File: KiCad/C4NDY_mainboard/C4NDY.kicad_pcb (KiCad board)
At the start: 2 copper layers, 22.9 x 50.2 mm, 46 parts, among them J1 Conn_01x08, J2 Conn_01x07, J3 Conn_01x05, J4 5077CR-16SMC2-BK-TR, J5 Conn_01x06, J6 Conn_01x08, J7 FTSH-105-01-L-DV-K, SW1 SKRPABE010, SW2 SKRPABE010, U1 MIC39100-3.3WS, U2 IS66WVS2M8BLL, U3 STM32G4A1CETx, X1 SG-310SCF

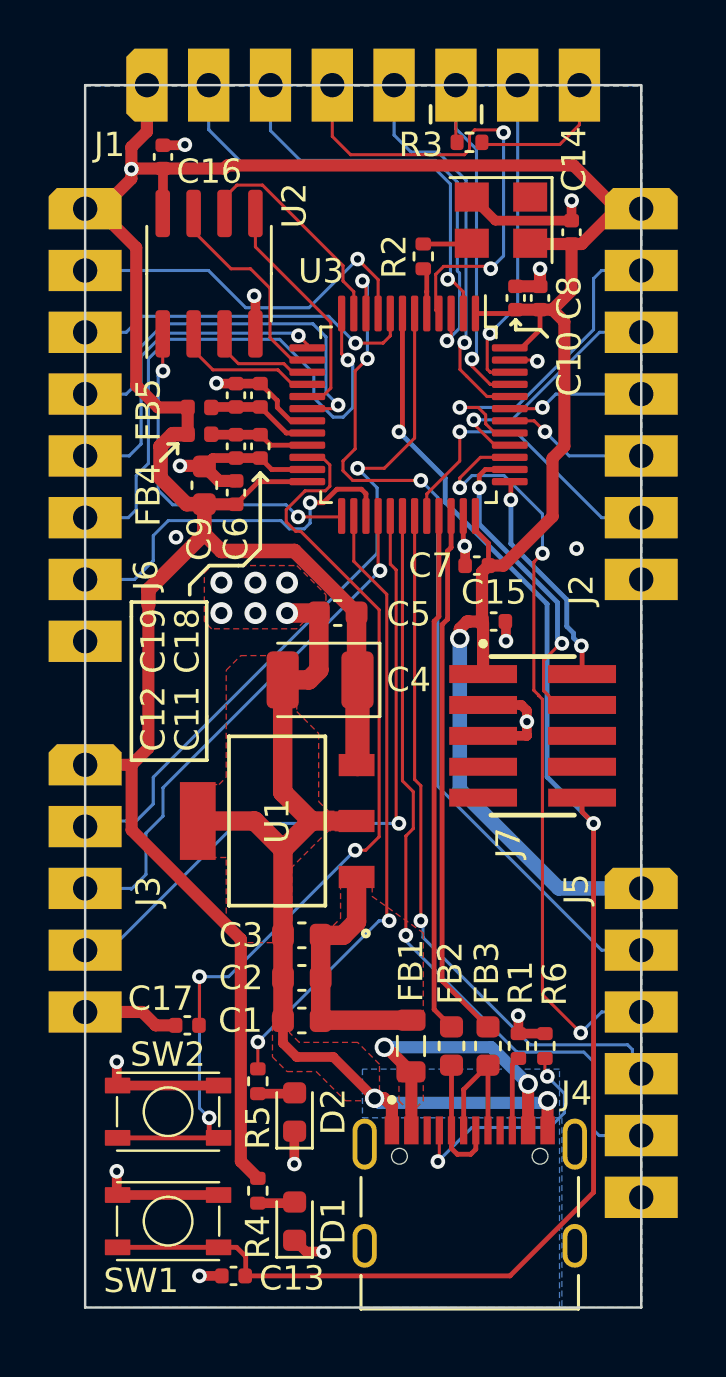
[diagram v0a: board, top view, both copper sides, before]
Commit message: SWD用のコネクタを汎用のピンヘッダに変更し、viaをテントに修正。
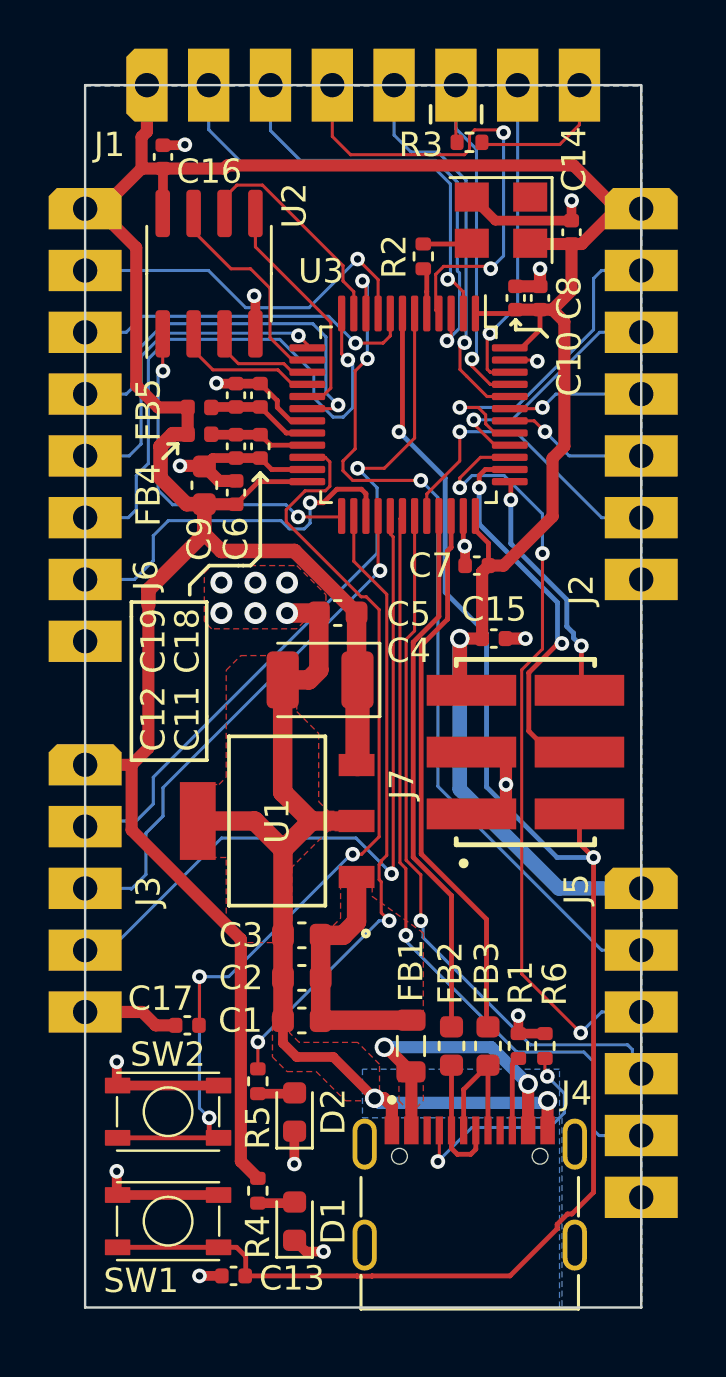
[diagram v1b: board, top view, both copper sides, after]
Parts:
- J4: value 5077CR-16SMC2-BK-TR -> UB1611-HGN; footprint My_Parts:NELTRON_5077CR-16SMC2-BK-TR -> My_Parts:Gangyuan_UB1611-HGN
- J7: value FTSH-105-01-L-DV-K -> 15910060; footprint My_Parts:SAMTEC_FTSH-105-XX-X-DV -> My_Parts:Molex_15910060
- moved J7 0.73 mm to (148.1, 107.2), turned to 90 degrees
- moved G*** 0.71 mm to (141.2, 104.4)
- moved C15 0.70 mm to (146.8, 102.5)
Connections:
- J7 pad 1: VCC -> GND
- J7 pad 2: /SWDIO -> /NRST
- J7 pad 5: GND -> VCC
- J7 pad 6: unconnected-(J7-Pin_6-Pad6) -> /SWDIO
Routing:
- net /SWCLK: track 13.5 -> 16.1 mm
- net /SPI_MOSI: track 26.8 -> 28.9 mm
- net /NRST: track 63.3 -> 65.1 mm
- net /SWDIO: track 9.14 -> 9.87 mm
- net /USB_DP: track 21.9 -> 22.6 mm
- net /USB_DM: track 21.8 -> 22.5 mm
- net GND: track 97.7 -> 98.3 mm, vias 26 -> 24
- net VCC: track 142.9 -> 142.7 mm, vias 2 -> 1
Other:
- board text added: "NRST"
- board text added: "SWCLK"
- board text added: "SWDIO"
- board text added: "VCC"
- board text added: "rev.D"
- board text removed: "SWD"
- board text removed: "rev.C"

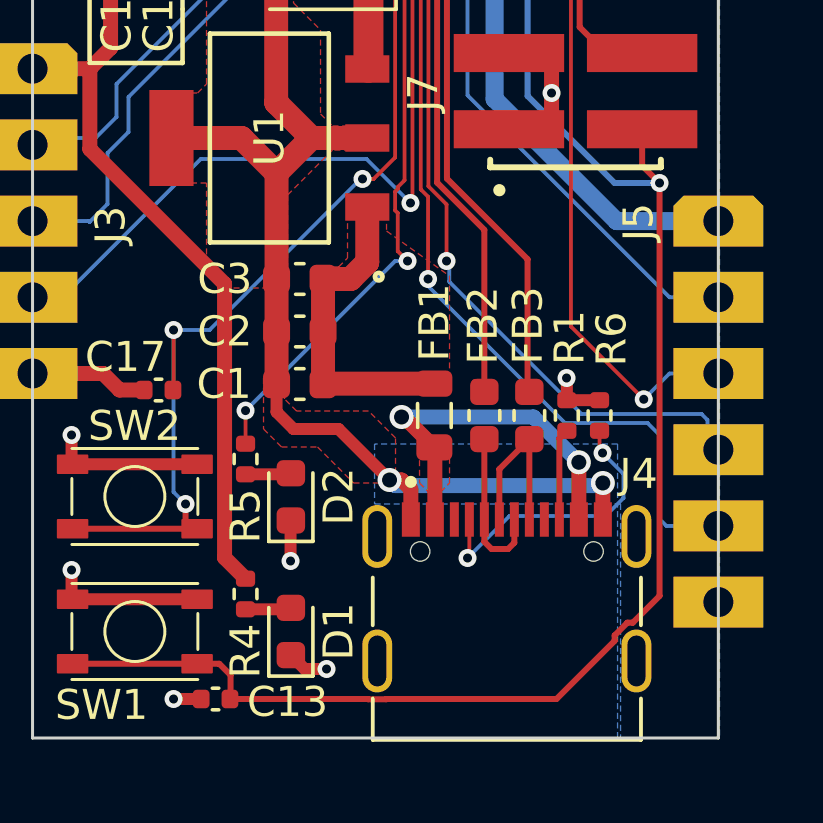
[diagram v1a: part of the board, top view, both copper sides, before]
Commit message: Modify USB Type-C Connector Position.
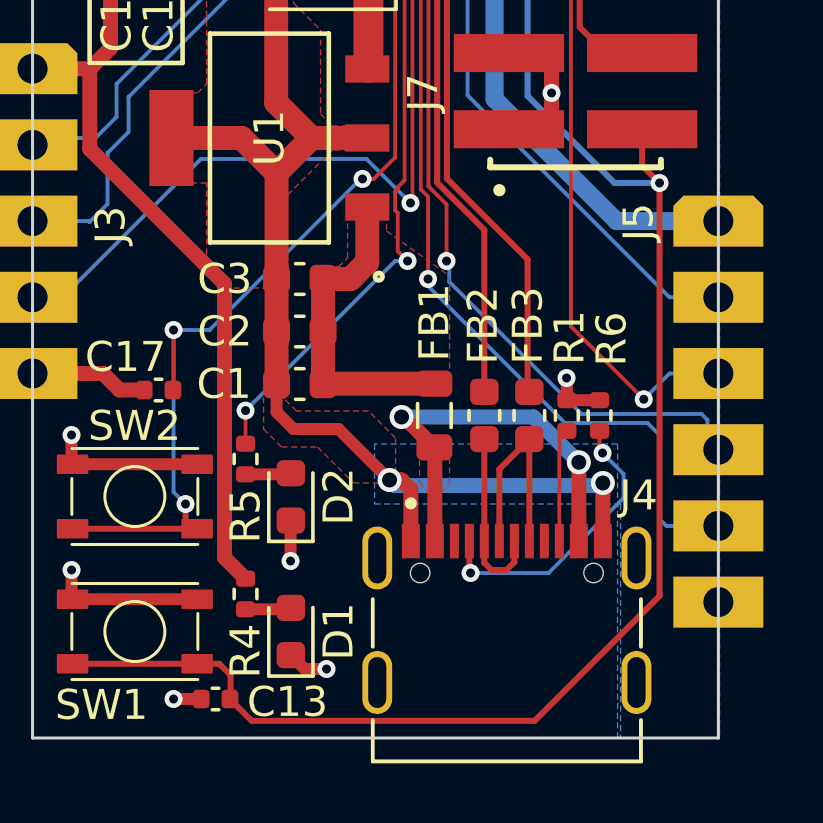
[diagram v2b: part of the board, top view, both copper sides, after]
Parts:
- moved J4 0.72 mm to (145.8, 124.5)
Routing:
- net GND: track 98.3 -> 100.3 mm
- net Net-(FB1-Pad1): track 12.4 -> 13.8 mm
- net /DP: track 5.77 -> 7.21 mm
- net Net-(J4-CC2): track 3.06 -> 3.78 mm
- net /DN: track 5.38 -> 6.04 mm
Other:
- board text added: "rev.F"
- board text removed: "rev.D"

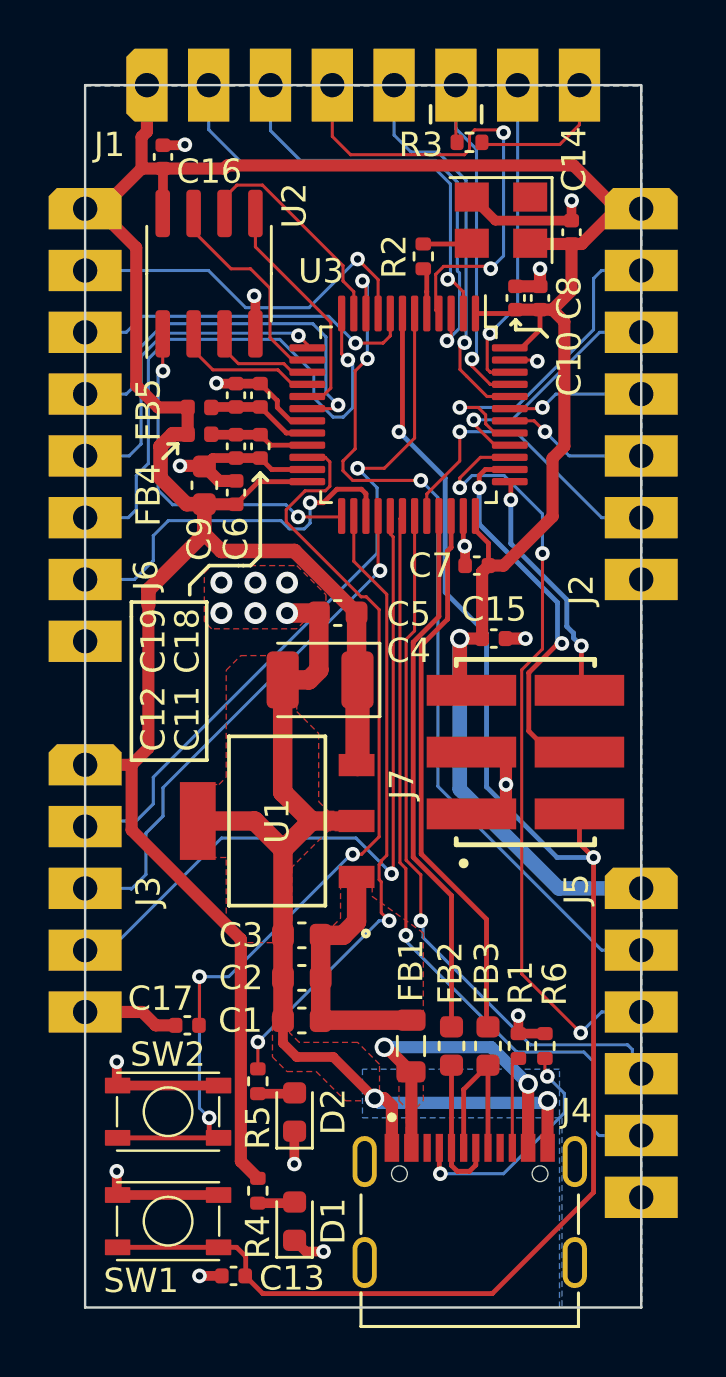
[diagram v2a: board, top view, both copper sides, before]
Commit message: Added TPS2116 and removed onboard QSPI..
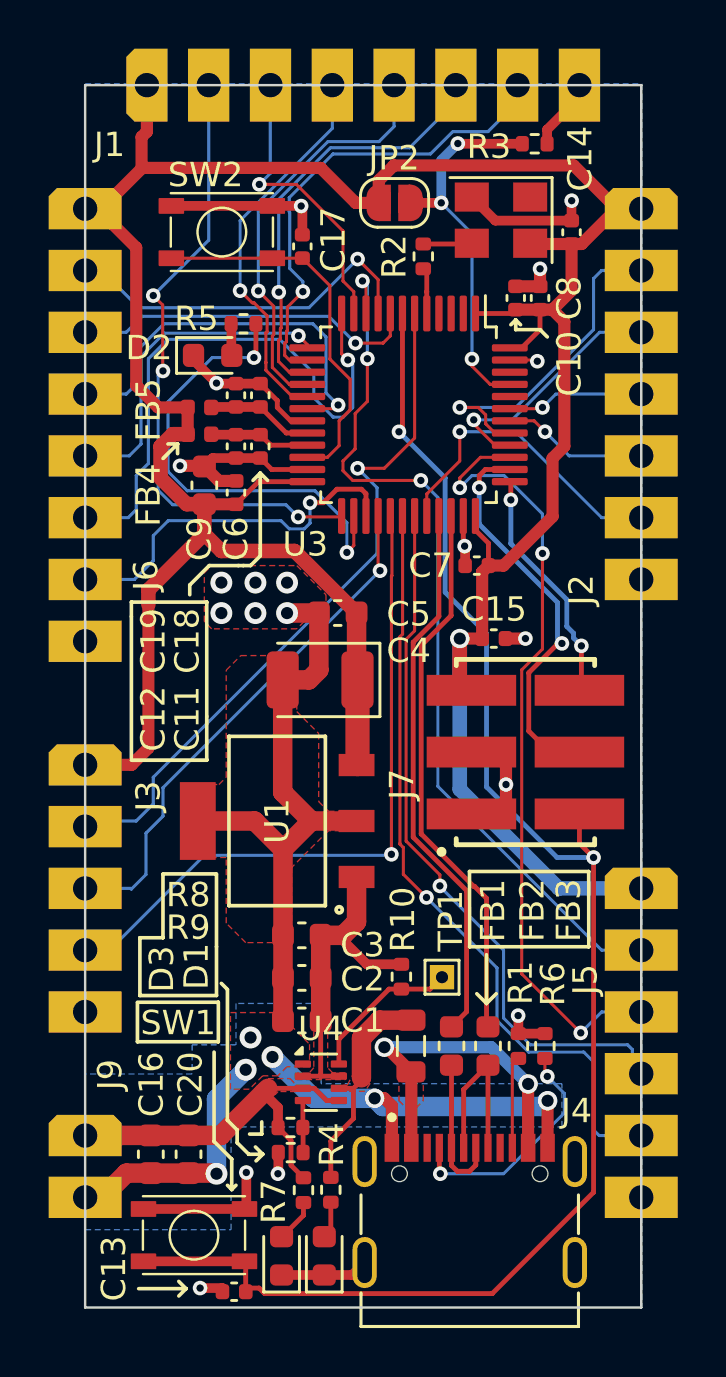
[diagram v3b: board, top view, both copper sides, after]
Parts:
- removed U2: IS66WVS2M8BLL, Package_SO:SOIC-8_3.9x4.9mm_P1.27mm
- added C20: 100nF, Capacitor_SMD:C_0603_1608Metric, F.Cu at (134.2, 123.7)
- added D3: LED, LED_SMD:LED_0603_1608Metric, F.Cu at (138.1, 127.9)
- added J9: Conn_01x02, My_Parts:PinHeader_1x02_P2.54mm_Vertical, F.Cu at (130.0, 122.9)
- added JP2: Jumper_2_Open, Jumper:SolderJumper-2_P1.3mm_Open_RoundedPad1.0x1.5mm, F.Cu at (142.7, 84.6)
- added R10: 10k, Resistor_SMD:R_0402_1005Metric, F.Cu at (143.0, 116.4)
- added R7: 1k, Resistor_SMD:R_0402_1005Metric, F.Cu at (139.0, 125.2)
- added R8: 16.9k, Resistor_SMD:R_0402_1005Metric, F.Cu at (138.4, 122.6)
- added R9: 5k, Resistor_SMD:R_0402_1005Metric, F.Cu at (138.4, 123.6)
- added TP1: TestPoint, TestPoint:TestPoint_THTPad_1.0x1.0mm_Drill0.5mm, F.Cu at (144.7, 116.4)
- added U4: TPS2116DRL, My_Parts:SOT-583-8, F.Cu at (139.7, 120.7)
- C16: value 100nF -> 10uF; footprint Capacitor_SMD:C_0402_1005Metric -> Capacitor_SMD:C_0603_1608Metric
- moved C16 41.0 mm to (132.7, 123.7), turned to -90 degrees
- moved SW2 36.2 mm to (135.6, 85.8)
- moved C17 32.4 mm to (138.9, 86.4), turned to 90 degrees
- moved D2 31.3 mm to (135.2, 90.9), turned to 0 degrees
- moved R5 31.1 mm to (136.5, 89.6), turned to 180 degrees
- moved R4 3.00 mm to (140.1, 125.2)
- moved R3 2.68 mm to (148.5, 82.2)
- moved D1 1.88 mm to (139.8, 127.9)
- moved SW1 1.21 mm to (134.5, 127.0)
- moved C13 0.65 mm to (136.1, 129.3)
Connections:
- C16 pad 1: VCC -> /PWR
- FB1 pad 2: VDD -> VBUS
- J1 pad 2: /PC13 -> /QSPI_NCS
- J1 pad 3: /PC14 -> /QSPI_CLK
- J1 pad 4: /PC15 -> /QSPI_IO0
- J1 pad 5: /PB7 -> /QSPI_IO1
- J1 pad 6: /BOOT0 -> /QSPI_IO2
- J1 pad 7: /PB9 -> /QSPI_IO3
- R4 pad 1: VCC -> VBUS
- U3 pad 2: /PC13 -> unconnected-(U3-PC13-Pad2)
- U3 pad 3: /PC14 -> unconnected-(U3-PC14-Pad3)
- U3 pad 4: /PC15 -> unconnected-(U3-PC15-Pad4)
- U3 pad 44: /PB7 -> unconnected-(U3-PB7-Pad44)
- U3 pad 46: /PB9 -> unconnected-(U3-PB9-Pad46)
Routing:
- net Net-(SW2-A): track 42.1 -> 15.6 mm, vias 3 -> 0
- net /PC15: track 19.8 -> 0.00 mm, vias 2 -> 0
- net VCC: track 142.7 -> 123.5 mm
- net /PC13: track 17.4 -> 0.00 mm, vias 1 -> 0
- net /PC14: track 17.4 -> 0.00 mm, vias 1 -> 0
- net /PB7: track 15.8 -> 0.00 mm, vias 1 -> 0
- net /PWR: track 0.00 -> 14.9 mm
- net /QSPI_IO2: track 4.44 -> 17.0 mm, vias 0 -> 1
- net /PB9: track 12.2 -> 0.00 mm, vias 1 -> 0
- net /QSPI_NCS: track 14.5 -> 25.7 mm, vias 2 -> 3
- net /QSPI_IO1: track 5.93 -> 16.9 mm, vias 0 -> 1
- net /QSPI_IO3: track 8.79 -> 19.4 mm, vias 0 -> 1
- net VBUS: track 0.00 -> 9.16 mm
- net GND: track 100.3 -> 107.1 mm, vias 24 -> 25
- net /QSPI_IO0: track 9.57 -> 16.2 mm, vias 0 -> 1
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- added copper zone on F.Cu, net /PWR
- added copper zone on F.Cu, net VBUS
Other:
- board text added: "15"
- board text added: "16"
- board text added: "21"
- board text added: "22"
- board text added: "28"
- board text added: "29"
- board text added: "36"
- board text added: "[PWR] VIN:14(5V only) VCC:1,9,21,28,36 GND:8,13,15,16,22,29 [ADC] 2:PA1/ADC12_IN2 3:PA0/ADC12_IN1 4:PB2/ADC2_IN12 5:PA5/ADC2_IN13 6:PA4/ADC2_IN17 7:PB13/ADC3_IN5 [SPI] 10:PF1/SPI2_SCK 11:PB14/SPI2_MISO 12:PB15/SPI2_MOSI [UART&I2C] 17:PA8/I2C2_SDA 18:PA9/I2C2_SCL 19:PA15/USART2_RX 20:PA2/USART2_TX [SAI] 23:PA10/SAI1_SD_A(DIN) 24:PB5/SAI1_SD_B(DOUT) 25:PB6/SAI1_FS_B(LRCLK) 26:PB3/SAI1_SCK_B(BCLK) 2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"
- board text added: "[QSPI] 30:PB11/QSPI_NCS 31:PA3/QSPI_CLK 32:PB1/QSPI_IO0 33:PB0/QSPI_IO1 34:PA7/QSPI_IO2 35:PA6/QSPI_IO3 [ONBOARD] D2:PB12/USER_LED SW:PB10/USER_SW JP2:PB8/BOOT0(10kpull-down) TP1:TPS2116 ST"
- board text added: "rev.G"
- board text removed: "19"
- board text removed: "20"
- board text removed: "26"
- board text removed: "27"
- board text removed: "34"
- board text removed: "3V3"
- board text removed: "A0/A12_1"
- board text removed: "A1/A12_2"
- board text removed: "A10/DIN"
- board text removed: "A15/RX"
- board text removed: "A2/TX"
- board text removed: "A4/A2_17"
- board text removed: "A5/A2_13"
- board text removed: "A8/SDA"
- board text removed: "A9/SCL"
- board text removed: "B10"
- board text removed: "B12"
- board text removed: "B13/A3_5"
- board text removed: "B14/MISO"
- board text removed: "B15/MOSI"
- board text removed: "B2/A2_12"
- board text removed: "B3/BCLK"
- board text removed: "B4/MCLK"
- board text removed: "B5/DOUT"
- board text removed: "B6/LRCLK"
- board text removed: "B7"
- board text removed: "B8/BOOT0"
- board text removed: "B9"
- board text removed: "C13"
- board text removed: "C14"
- board text removed: "C15"
- board text removed: "F1/SCK"
- board text removed: "G"
- board text removed: "GND"
- board text removed: "NRST"
- board text removed: "PWR"
- board text removed: "RST"
- board text removed: "SWCLK"
- board text removed: "SWDIO"
- board text removed: "VCC"
- board text removed: "[OTHER] 28:PB9 29:PB8/BOOT0(10k pull-down) 30:PB7 31:PC15 32:PC14 33:C13 [ONBOARD] LED:PB12 SW:PB10 QSPI_NCS:PB11 QSPI_CLK:PA3 QSPI_IO0:PB1 QSPI_IO1:PB0 QSPI_IO2:PA7 QSPI_IO3:PA6"
- board text removed: "[PWR] VCC:1,9,19,26,34 GND:8,13,14,20,27 [ADC] 2:PA1/ADC12_IN2 3:PA0/ADC12_IN1 4:PB2/ADC2_IN12 5:PA5/ADC2_IN13 6:PA4/ADC2_IN17 7:PB13/ADC3_IN5 [SPI] 10:PF1/SPI2_SCK 11:PB14/SPI2_MISO 12:PB15/SPI2_MOSI [UART&I2C] 15:PA8/I2C2_SDA 16:PA9/I2C2_SCL 17:PA15/USART2_RX 18:PA2/USART2_TX [SAI] 21:PA10/SAI1_SD_A(DIN) 22:PB5/SAI1_SD_B(DOUT) 23:PB6/SAI1_FS_B(LRCLK) 24:PB3/SAI1_SCK_B(BCLK) 25:PB4/SAI1_MCLK_B"
- board text removed: "rev.F"
